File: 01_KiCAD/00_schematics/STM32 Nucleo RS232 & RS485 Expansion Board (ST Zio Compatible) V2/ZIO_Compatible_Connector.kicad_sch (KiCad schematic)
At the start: 11 parts, among them CN10 Conn_02x17_Odd_Even, CN7 Conn_02x10_Odd_Even, CN8 Conn_02x08_Odd_Even, CN9 Conn_02x15_Odd_Even

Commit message: Final revision checkup
After BOM-update and corrected some footprints and package sizes for resistors and capacitors, updated the PCB to "HW REV A0.2" as final PCB layout. Need to run DRC check before final approval.
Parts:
- CN10: value Conn_02x17_Odd_Even -> SSW-117-23-G-D; Mouser PN (none) -> 200-SSW11723GD
- CN7: value Conn_02x10_Odd_Even -> SSW-110-23-G-D; Mouser PN (none) -> 200-SSW11023GD
- CN8: value Conn_02x08_Odd_Even -> SSW-108-23-G-D; Mouser PN (none) -> 200-SSW10823GD
- CN9: value Conn_02x15_Odd_Even -> SSW-115-23-G-D; Mouser PN (none) -> 200-SSW11523GD; Package (none) -> Through Hole,P=2.54mm; Type (none) -> THT
- R70, R71, R72, R73, R74, R75, R76: LCSC C105881 -> C513549; MPN RC0603FR-07330RL -> AC0603FR-7W330RL; Mouser PN (none) -> 603-AC0603FR-7W330RL
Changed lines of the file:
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@@
 			)
 		)
-		(property "Datasheet" "~"
+		(property "Datasheet" "https://www.lcsc.com/datasheet/C513549.pdf"
 			(at 71.12 102.87 0)
 			(effects
@@
 			)
 		)
-		(property "Description" "Resistor"
+		(property "Description" "330Ω ±1% 200mW 0603 Thick Film Resistor"
 			(at 71.12 102.87 0)
 			(effects
@@
 			)
 		)
-		(property "MPN" "RC0603FR-07330RL"
+		(property "MPN" "AC0603FR-7W330RL"
 			(at 71.12 102.87 0)
 			(effects
@@
 			)
 		)
-		(property "LCSC" "C105881"
+		(property "LCSC" "C513549"
 			(at 71.12 102.87 0)
 			(effects
@@
 		)
 		(property "MOUSER_PART_NUMBER" ""
+			(at 71.12 102.87 90)
+			(effects
+				(font
+					(size 1.27 1.27)
+				)
+				(hide yes)
+			)
+		)
+		(property "Mouser PN" "603-AC0603FR-7W330RL"
 			(at 71.12 102.87 90)
 			(effects
@@
 			)
 		)
-		(property "Datasheet" "~"
+		(property "Datasheet" "https://www.lcsc.com/datasheet/C513549.pdf"
 			(at 87.63 97.79 0)
 			(effects
@@
 			)
 		)
-		(property "Description" "Resistor"
+		(property "Description" "330Ω ±1% 200mW 0603 Thick Film Resistor"
 			(at 87.63 97.79 0)
 			(effects
@@
 			)
 		)
-		(property "MPN" "RC0603FR-07330RL"
+		(property "MPN" "AC0603FR-7W330RL"
 			(at 87.63 97.79 0)
 			(effects
@@
 			)
 		)
-		(property "LCSC" "C105881"
+		(property "LCSC" "C513549"
 			(at 87.63 97.79 0)
 			(effects
@@
 		)
 		(property "MOUSER_PART_NUMBER" ""
+			(at 87.63 97.79 90)
+			(effects
+				(font
+					(size 1.27 1.27)
+				)
+				(hide yes)
+			)
+		)
+		(property "Mouser PN" "603-AC0603FR-7W330RL"
 			(at 87.63 97.79 90)
 			(effects
@@
 			)
 		)
-		(property "Value" "Conn_02x15_Odd_Even"
+		(property "Value" "SSW-115-23-G-D"
 			(at 105.41 93.98 0)
 			(effects
@@
 			)
 		)
-		(property "Datasheet" "~"
+		(property "Datasheet" "https://www.lcsc.com/datasheet/C7089189.pdf"
 			(at 104.14 115.57 0)
 			(effects
@@
 			)
 		)
-		(property "Description" "Generic connector, double row, 02x15, odd/even pin numbering scheme (row 1 odd numbers, row 2 even numbers), script generated (kicad-library-utils/schlib/autogen/connector/)"
+		(property "Description" "Female Header 30 Position 2.54mm Pitch Dual Row Through Hole -55℃~+125℃"
 			(at 104.14 115.57 0)
 			(effects
@@
 			)
 		)
-		(property "Package" ""
+		(property "Package" "Through Hole,P=2.54mm"
 			(at 104.14 115.57 0)
 			(effects
@@
 			)
 		)
-		(property "Type" ""
+		(property "Type" "THT"
 			(at 104.14 115.57 0)
 			(effects
@@
 		)
 		(property "MOUSER_PART_NUMBER" ""
+			(at 104.14 115.57 0)
+			(effects
+				(font
+					(size 1.27 1.27)
+				)
+				(hide yes)
+			)
+		)
+		(property "Mouser PN" "200-SSW11523GD"
 			(at 104.14 115.57 0)
 			(effects
@@
 			)
 		)
-		(property "Datasheet" "~"
+		(property "Datasheet" "https://www.lcsc.com/datasheet/C513549.pdf"
 			(at 198.12 77.47 0)
 			(effects
@@
 			)
 		)
-		(property "Description" "Resistor"
+		(property "Description" "330Ω ±1% 200mW 0603 Thick Film Resistor"
 			(at 198.12 77.47 0)
 			(effects
@@
 			)
 		)
-		(property "MPN" "RC0603FR-07330RL"
+		(property "MPN" "AC0603FR-7W330RL"
 			(at 198.12 77.47 0)
 			(effects
@@
 			)
 		)
-		(property "LCSC" "C105881"
+		(property "LCSC" "C513549"
 			(at 198.12 77.47 0)
 			(effects
@@
 		)
 		(property "MOUSER_PART_NUMBER" ""
+			(at 198.12 77.47 90)
+			(effects
+				(font
+					(size 1.27 1.27)
+				)
+				(hide yes)
+			)
+		)
+		(property "Mouser PN" "603-AC0603FR-7W330RL"
 			(at 198.12 77.47 90)
 			(effects
@@
 			)
 		)
-		(property "Datasheet" "~"
+		(property "Datasheet" "https://www.lcsc.com/datasheet/C513549.pdf"
 			(at 87.63 105.41 0)
 			(effects
@@
 			)
 		)
-		(property "Description" "Resistor"
+		(property "Description" "330Ω ±1% 200mW 0603 Thick Film Resistor"
 			(at 87.63 105.41 0)
 			(effects
@@
 			)
 		)
-		(property "MPN" "RC0603FR-07330RL"
+		(property "MPN" "AC0603FR-7W330RL"
 			(at 87.63 105.41 0)
 			(effects
@@
 			)
 		)
-		(property "LCSC" "C105881"
+		(property "LCSC" "C513549"
 			(at 87.63 105.41 0)
 			(effects
@@
 		)
 		(property "MOUSER_PART_NUMBER" ""
+			(at 87.63 105.41 90)
+			(effects
+				(font
+					(size 1.27 1.27)
+				)
+				(hide yes)
+			)
+		)
+		(property "Mouser PN" "603-AC0603FR-7W330RL"
 			(at 87.63 105.41 90)
 			(effects
@@
 			)
 		)
-		(property "Datasheet" "~"
+		(property "Datasheet" "https://www.lcsc.com/datasheet/C513549.pdf"
 			(at 71.12 107.95 0)
 			(effects
@@
 			)
 		)
-		(property "Description" "Resistor"
+		(property "Description" "330Ω ±1% 200mW 0603 Thick Film Resistor"
 			(at 71.12 107.95 0)
 			(effects
@@
 			)
 		)
-		(property "MPN" "RC0603FR-07330RL"
+		(property "MPN" "AC0603FR-7W330RL"
 			(at 71.12 107.95 0)
 			(effects
@@
 			)
 		)
-		(property "LCSC" "C105881"
+		(property "LCSC" "C513549"
 			(at 71.12 107.95 0)
 			(effects
@@
 		)
 		(property "MOUSER_PART_NUMBER" ""
+			(at 71.12 107.95 90)
+			(effects
+				(font
+					(size 1.27 1.27)
+				)
+				(hide yes)
+			)
+		)
+		(property "Mouser PN" "603-AC0603FR-7W330RL"
 			(at 71.12 107.95 90)
 			(effects
@@
 			)
 		)
-		(property "Datasheet" "~"
+		(property "Datasheet" "https://www.lcsc.com/datasheet/C513549.pdf"
 			(at 198.12 64.77 0)
 			(effects
@@
 			)
 		)
-		(property "Description" "Resistor"
+		(property "Description" "330Ω ±1% 200mW 0603 Thick Film Resistor"
 			(at 198.12 64.77 0)
 			(effects
@@
 			)
 		)
-		(property "MPN" "RC0603FR-07330RL"
+		(property "MPN" "AC0603FR-7W330RL"
 			(at 198.12 64.77 0)
 			(effects
@@
 			)
 		)
-		(property "LCSC" "C105881"
+		(property "LCSC" "C513549"
 			(at 198.12 64.77 0)
 			(effects
@@
 		)
 		(property "MOUSER_PART_NUMBER" ""
+			(at 198.12 64.77 90)
+			(effects
+				(font
+					(size 1.27 1.27)
+				)
+				(hide yes)
+			)
+		)
+		(property "Mouser PN" "603-AC0603FR-7W330RL"
 			(at 198.12 64.77 90)
 			(effects
@@
 			)
 		)
-		(property "Value" "Conn_02x10_Odd_Even"
+		(property "Value" "SSW-110-23-G-D"
 			(at 182.88 50.8 0)
 			(effects
@@
 			)
 		)
-		(property "Datasheet" "~"
+		(property "Datasheet" "https://www.lcsc.com/datasheet/C6236460.pdf"
 			(at 181.61 64.77 0)
 			(effects
@@
 			)
 		)
-		(property "Description" "Generic connector, double row, 02x10, odd/even pin numbering scheme (row 1 odd numbers, row 2 even numbers), script generated (kicad-library-utils/schlib/autogen/connector/)"
+		(property "Description" "Female Header 20 Position 2.54mm Pitch Dual Row Through Hole -55℃~+125℃"
 			(at 181.61 64.77 0)
 			(effects
@@
 		)
 		(property "MOUSER_PART_NUMBER" ""
+			(at 181.61 64.77 0)
+			(effects
+				(font
+					(size 1.27 1.27)
+				)
+				(hide yes)
+			)
+		)
+		(property "Mouser PN" "200-SSW11023GD"
 			(at 181.61 64.77 0)
 			(effects
@@
 			)
 		)
-		(property "Value" "Conn_02x08_Odd_Even"
+		(property "Value" "SSW-108-23-G-D"
 			(at 105.41 60.9973 0)
 			(effects
@@
 			)
 		)
-		(property "Datasheet" "~"
+		(property "Datasheet" "https://www.lcsc.com/datasheet/C7019040.pdf"
 			(at 104.14 72.39 0)
 			(effects
@@
 			)
 		)
-		(property "Description" "Generic connector, double row, 02x08, odd/even pin numbering scheme (row 1 odd numbers, row 2 even numbers), script generated (kicad-library-utils/schlib/autogen/connector/)"
+		(property "Description" "Female Header 16 Position 2.54mm Pitch Dual Row Through Hole -55℃~+125℃"
 			(at 104.14 72.39 0)
 			(effects
@@
 		)
 		(property "MOUSER_PART_NUMBER" ""
+			(at 104.14 72.39 0)
+			(effects
+				(font
+					(size 1.27 1.27)
+				)
+				(hide yes)
+			)
+		)
+		(property "Mouser PN" "200-SSW10823GD"
 			(at 104.14 72.39 0)
 			(effects
@@
 			)
 		)
-		(property "Datasheet" "~"
+		(property "Datasheet" "https://www.lcsc.com/datasheet/C513549.pdf"
 			(at 198.12 92.71 0)
 			(effects
@@
 			)
 		)
-		(property "Description" "Resistor"
+		(property "Description" "330Ω ±1% 200mW 0603 Thick Film Resistor"
 			(at 198.12 92.71 0)
 			(effects
@@
 			)
 		)
-		(property "MPN" "RC0603FR-07330RL"
+		(property "MPN" "AC0603FR-7W330RL"
 			(at 198.12 92.71 0)
 			(effects
@@
 			)
 		)
-		(property "LCSC" "C105881"
+		(property "LCSC" "C513549"
 			(at 198.12 92.71 0)
 			(effects
@@
 		)
 		(property "MOUSER_PART_NUMBER" ""
+			(at 198.12 92.71 90)
+			(effects
+				(font
+					(size 1.27 1.27)
+				)
+				(hide yes)
+			)
+		)
+		(property "Mouser PN" "603-AC0603FR-7W330RL"
 			(at 198.12 92.71 90)
 			(effects
@@
 			)
 		)
-		(property "Value" "Conn_02x17_Odd_Even"
+		(property "Value" "SSW-117-23-G-D"
 			(at 182.88 88.9 0)
 			(effects
@@
 			)
 		)
-		(property "Datasheet" "~"
+		(property "Datasheet" "https://www.lcsc.com/datasheet/C6501751.pdf"
 			(at 181.61 113.03 0)
 			(effects
@@
 			)
 		)
-		(property "Description" "Generic connector, double row, 02x17, odd/even pin numbering scheme (row 1 odd numbers, row 2 even numbers), script generated (kicad-library-utils/schlib/autogen/connector/)"
+		(property "Description" "Female Header 34 Position 2.54mm Pitch Dual Row Through Hole -55℃~+125℃"
 			(at 181.61 113.03 0)
 			(effects
@@
 			(at 181.61 113.03 0)
 			(effects
+				(font
+					(size 1.27 1.27)
+				)
+				(hide yes)
+			)
+		)
+		(property "Mouser PN" "200-SSW11723GD"
+			(at 181.61 113.03 0)
+			(effects

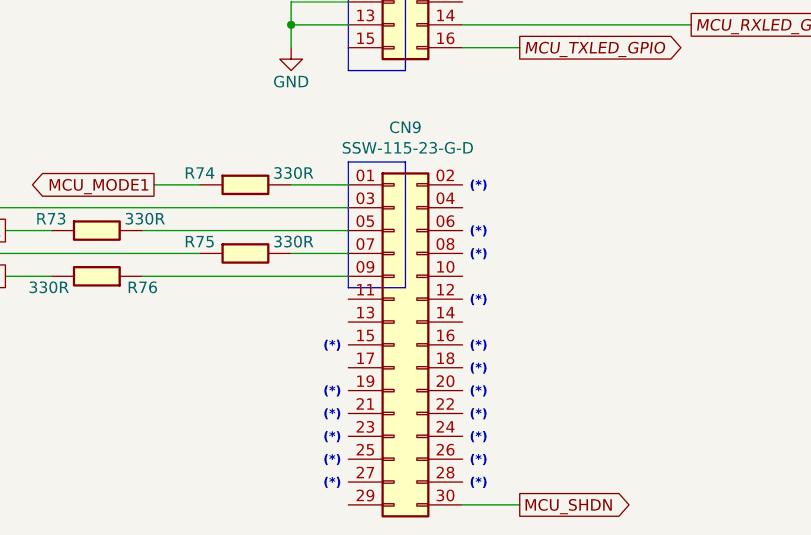
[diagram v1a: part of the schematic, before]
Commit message: Changed to HR_REVA0.3
Updates design to PCB HW-REVA0.3 with the folowing changes:

CL_HW_2026_0001
Replaced text on silkscreen D3=>RX and D4=>TX.

CL_HW_2026_0002
Changed MCU_SHDN pin for THVD4431 from CN9-30 to CN9-11 to make it also Arduino compatible
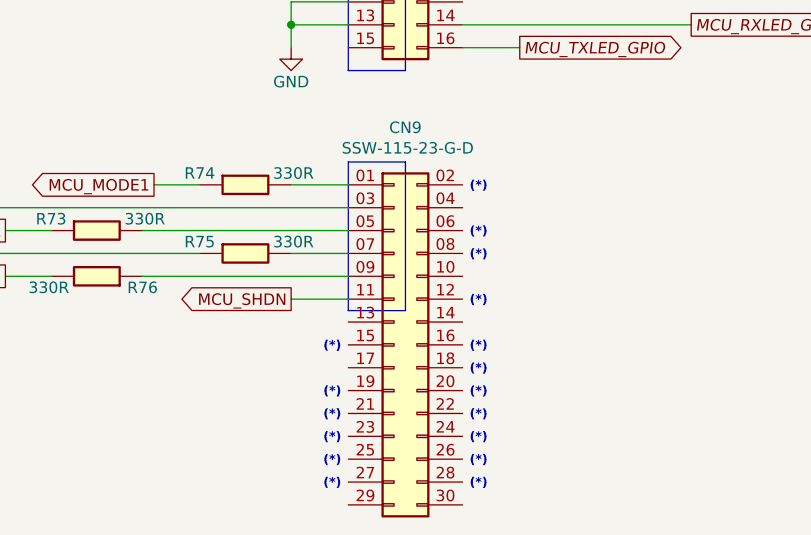
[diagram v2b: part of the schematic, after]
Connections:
- net MCU_SHDN: now also CN9.11 (Pin_11); no longer CN9.30 (Pin_30)
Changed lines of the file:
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@@
 	(rectangle
 		(start 99.06 95.25)
-		(end 105.41 109.22)
+		(end 105.41 111.76)
 		(stroke
 			(width 0)
@@
 	(wire
 		(pts
+			(xy 92.71 110.49) (xy 99.06 110.49)
+		)
+		(stroke
+			(width 0)
+			(type default)
+		)
+	)
+	(wire
+		(pts
 			(xy 195.58 100.33) (xy 189.23 100.33)
 		)
@@
 		(pts
 			(xy 195.58 69.85) (xy 189.23 69.85)
-		)
-		(stroke
-			(width 0)
-			(type default)
-		)
-	)
-	(wire
-		(pts
-			(xy 118.11 133.35) (xy 111.76 133.35)
 		)
 		(stroke
@@
 	(global_label "MCU_SHDN"
 		(shape output)
-		(at 118.11 133.35 0)
+		(at 92.71 110.49 180)
 		(fields_autoplaced yes)
 		(effects
@@
 				(size 1.27 1.27)
 			)
-			(justify left)
+			(justify right)
 		)
 		(property "Intersheetrefs" "${INTERSHEET_REFS}"
-			(at 131.2552 133.35 0)
+			(at 79.5648 110.49 0)
 			(effects
 				(font
 					(size 1.27 1.27)
 				)
-				(justify left)
+				(justify right)
 				(hide yes)
 			)
